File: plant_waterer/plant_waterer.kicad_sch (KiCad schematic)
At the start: 25 parts, among them J2 Conn_01x02, J3 PJ-002AH, J4 Conn_01x03, U1 ZXBM5210-SP-13, U2 OLED_DISP, U4 ESD7002, U5 AP2204R-5.0TRG1, U6 PicoW

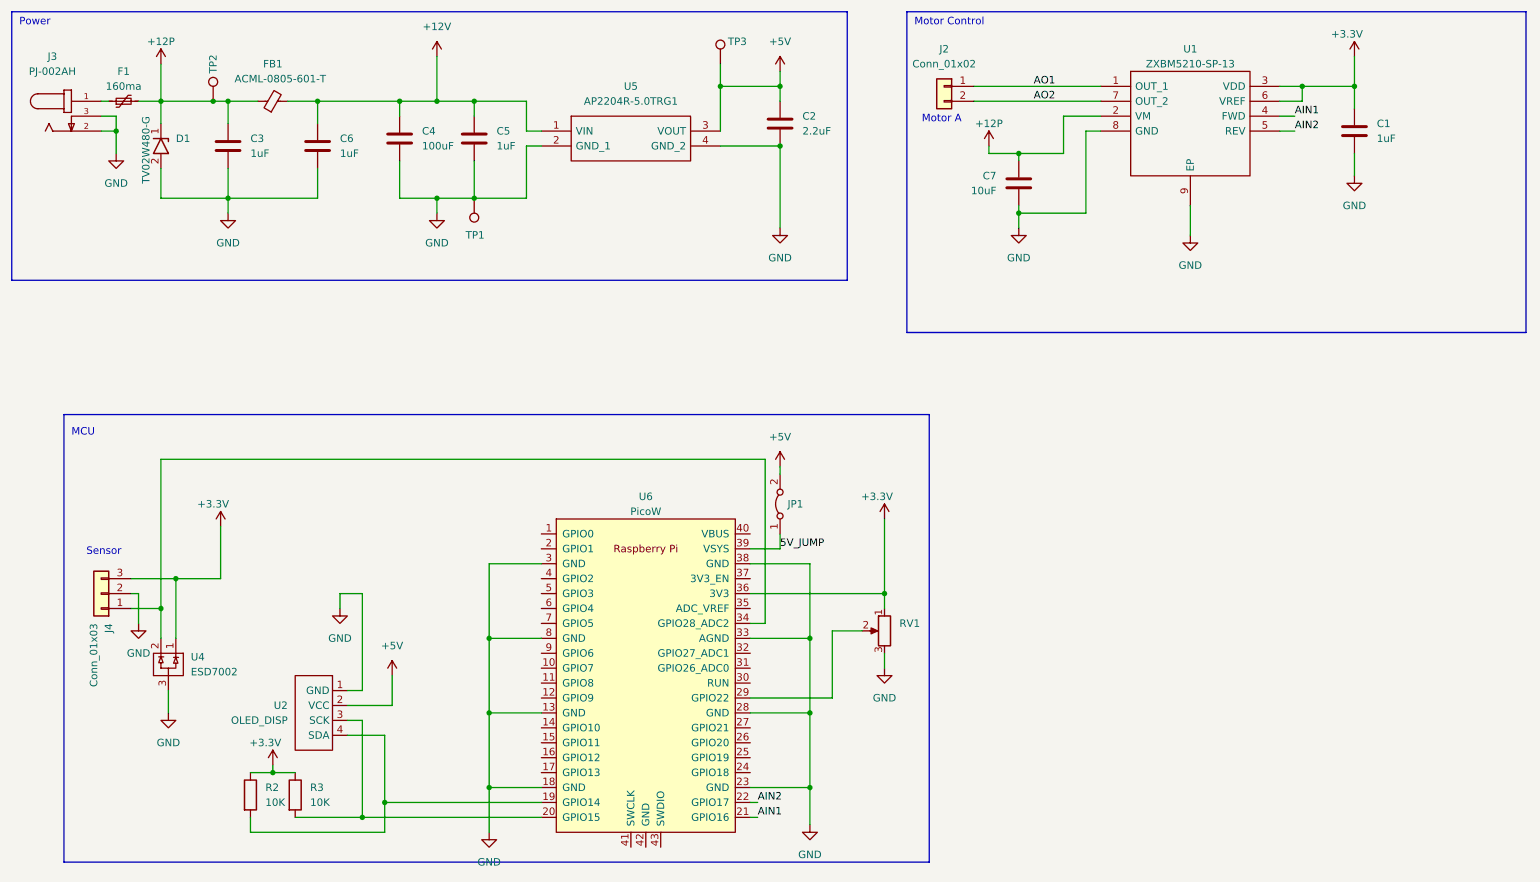
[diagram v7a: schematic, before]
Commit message: Added off board connectors for I2C
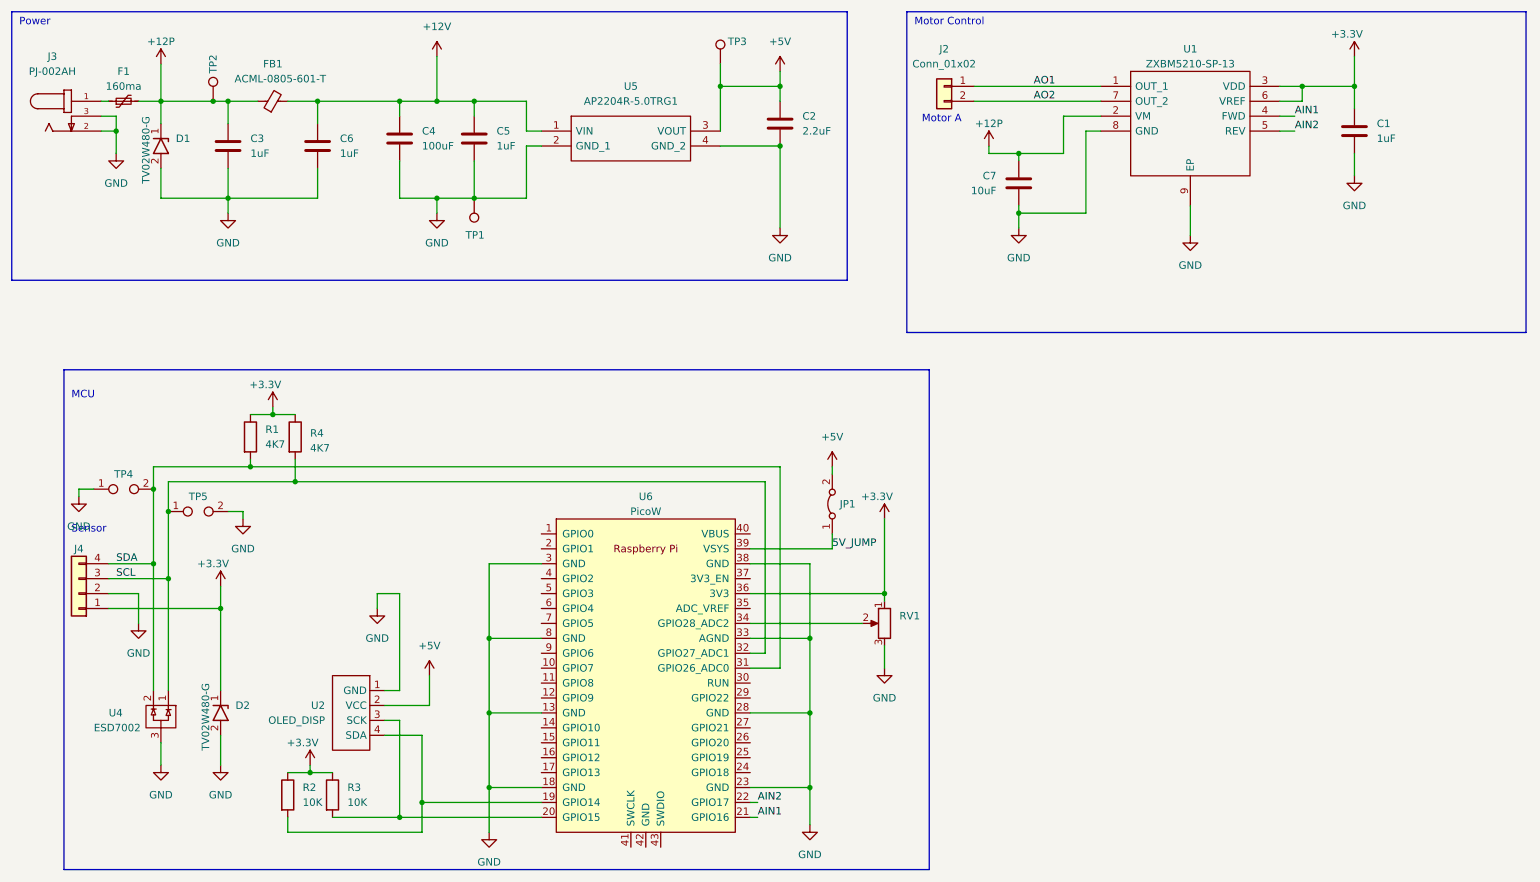
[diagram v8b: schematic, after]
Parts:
- added D2: TV02W480-G, Diode_SMD:D_SOD-123, symbol MySymbols:TV02W480-G
- added R1, R4: 4K7, Resistor_SMD:R_0805_2012Metric_Pad1.20x1.40mm_HandSolder, symbol Device:R
- added TP4, TP5: TestPoint_2Pole, TestPoint:TestPoint_2Pads_Pitch5.08mm_Drill1.3mm, symbol Connector:TestPoint_2Pole
- J4: footprint Library:TE-282841-3-0 -> Connector_PinSocket_2.54mm:PinSocket_1x04_P2.54mm_Vertical; symbol Connector_Generic:Conn_01x03 -> Connector_Generic:Conn_01x04
- TP1: footprint TestPoint:TestPoint_Loop_D1.80mm_Drill1.0mm_Beaded -> TestPoint:TestPoint_2Pads_Pitch5.08mm_Drill1.3mm
- U1: footprint Package_SO:SOIC-8-1EP_3.9x4.9mm_P1.27mm_EP2.41x3.81mm_ThermalVias -> Package_SO:SOIC-8-1EP_3.9x4.9mm_P1.27mm_EP2.41x3.81mm
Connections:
- net +3.3V: now also J4.1 (Pin_1), D2.1, R1.1, R4.1; no longer J4.3 (Pin_3), U4.1
- net GND: now also D2.2, TP4.1, TP5.2
- net at RV1.2: now also U6.34 (GPIO28_ADC2); no longer U6.29 (GPIO22)
- net SDA: now reaches U6.31 (GPIO26_ADC0)
- net SDA: now also J4.4 (Pin_4), U4.2, R1.2, TP4.2
- net SCL: now reaches U6.32 (GPIO27_ADC1)
- net SCL: now also J4.3 (Pin_3), U4.1, R4.2, TP5.1
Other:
- moved on the sheet: JP1, R2, R3, RV1, U2, U4
